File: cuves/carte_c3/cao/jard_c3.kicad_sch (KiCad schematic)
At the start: 24 parts, among them J1 Connecteur, J2 LEDs, Q1 BPC_IPP034N03L, U1 ESP32-C3_SUPERMINI_TH, U2 BPC_Alim3_3V, X1 Trou, X2 Trou

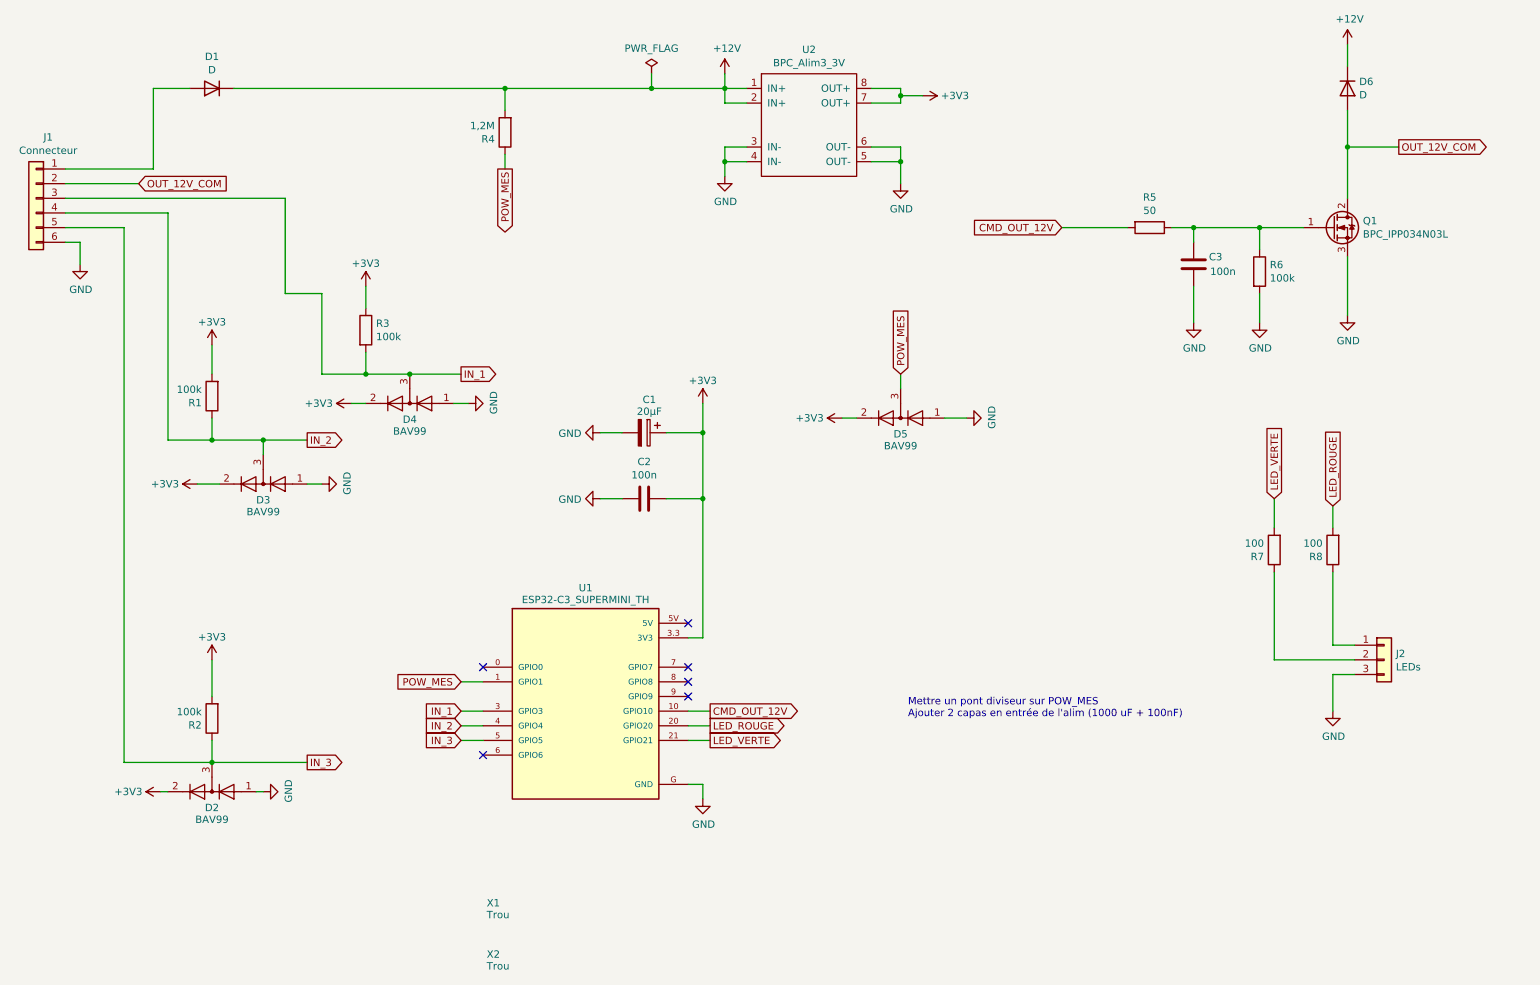
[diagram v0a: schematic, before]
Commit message: Changement de la forme de la carte: Boîte 85 x 85 x 55
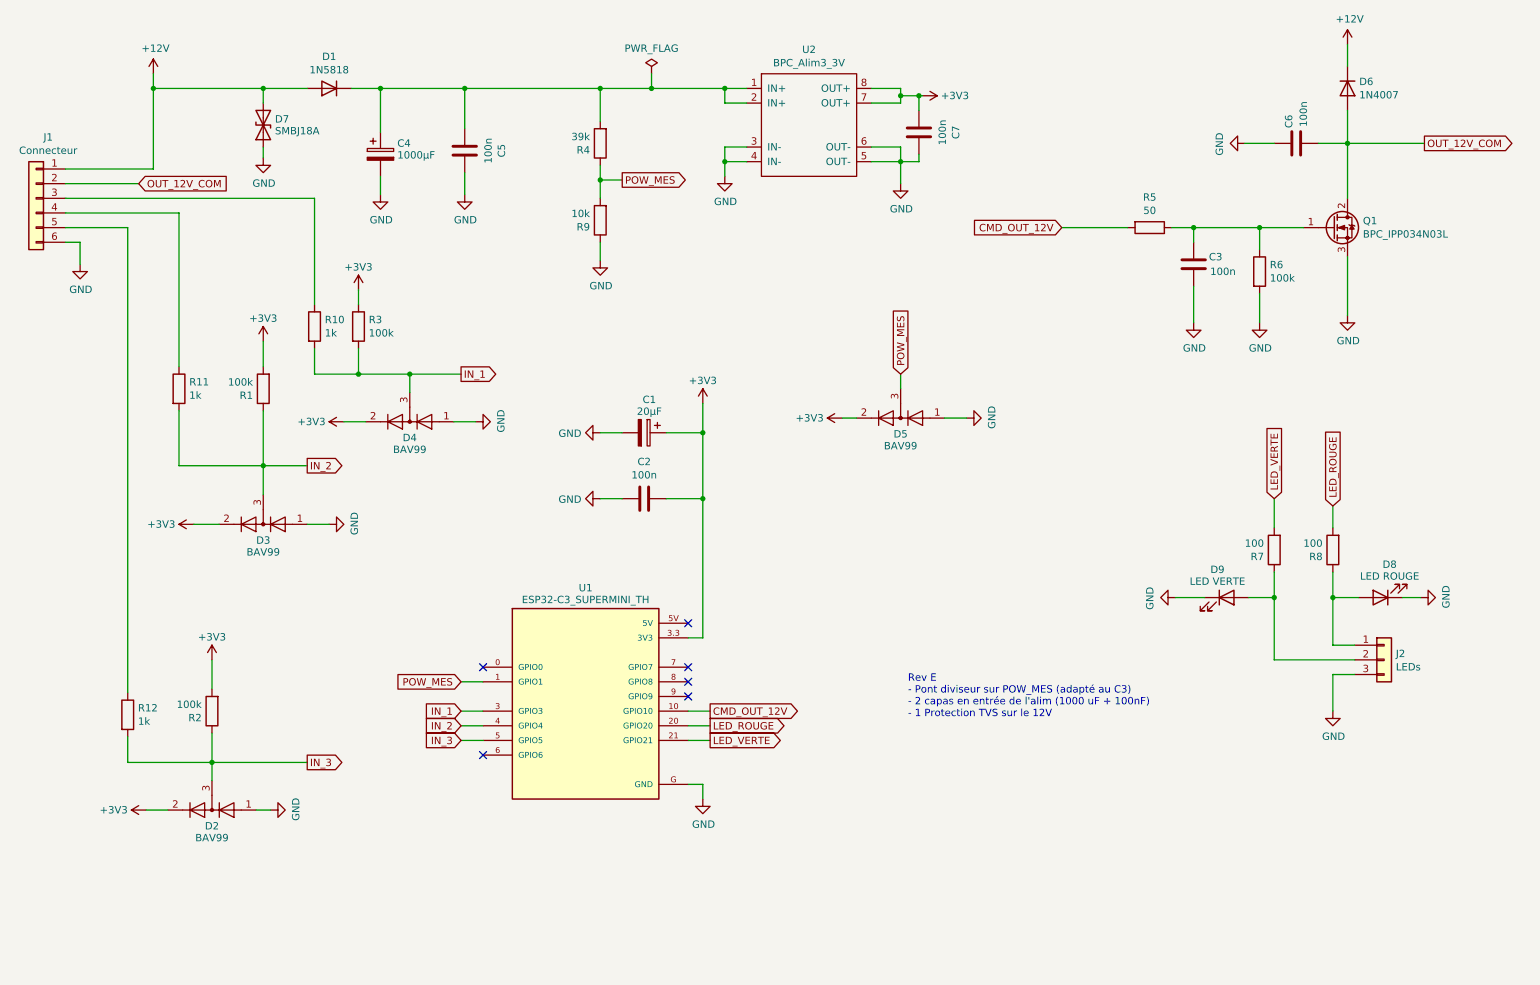
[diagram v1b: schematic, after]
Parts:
- removed X1, X2: Trou, bpc:BPC_Trou4mm_Fixation, symbol bpc:BPC_TROU
- added C4: 1000µF, Capacitor_THT:C_Radial_D16.0mm_H25.0mm_P7.50mm, symbol Device:C_Polarized
- added C5, C6, C7: 100n, Capacitor_SMD:C_0805_2012Metric_Pad1.18x1.45mm_HandSolder, symbol Device:C
- added D7: SMBJ18A, Diode_SMD:D_SMB_Handsoldering, symbol Device:D_TVS
- added D8: LED ROUGE, LED_THT:LED_D3.0mm, symbol Device:LED
- added D9: LED VERTE, LED_THT:LED_D3.0mm, symbol Device:LED
- added R10, R11, R12: 1k, Resistor_SMD:R_0805_2012Metric_Pad1.20x1.40mm_HandSolder, symbol Device:R
- added R9: 10k, Resistor_SMD:R_0805_2012Metric_Pad1.20x1.40mm_HandSolder, symbol Device:R
- D1: value D -> 1N5818; footprint Diode_THT:D_A-405_P2.54mm_Vertical_KathodeUp -> Diode_THT:D_DO-41_SOD81_P10.16mm_Horizontal
- D6: value D -> 1N4007
- R4: value 1,2M -> 39k
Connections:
- net +12V: now also D1.2 (A), J1.1 (Pin_1), D7.2 (A2); no longer D1.1 (K), R4.2, U2.1 (IN+), U2.2 (IN+)
- net +3V3: now also C7.2
- net GND: now also C4.2, C5.1, C6.1, C7.1, D7.1 (A1), D8.1 (K), D9.1 (K), R9.1
- net IN_1: now also R10.2; no longer J1.3 (Pin_3)
- net IN_2: now also R11.2; no longer J1.4 (Pin_4)
- net IN_3: now also R12.2; no longer J1.5 (Pin_5)
- net OUT_12V_COM: now also C6.2
- net POW_MES: now also R9.2
- net at J2.2 (Pin_2), R7.1: now also D9.2 (A)
- net at J2.1 (Pin_1), R8.1: now also D8.2 (A)
- new net: J1.3 (Pin_3), R10.1
- new net: J1.4 (Pin_4), R11.1
- new net: J1.5 (Pin_5), R12.1
- new net: C4.1, C5.2, D1.1 (K), R4.2, U2.1 (IN+), U2.2 (IN+)
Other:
- note added: "Rev E - Pont diviseur sur POW_MES (adapté au C3) - 2 capas en entrée de l'alim (1000 uF + 100nF) - 1 Protection TVS sur le 12V"
- note removed: "Mettre un pont diviseur sur POW_MES Ajouter 2 capas en entrée de l'alim (1000 uF + 100nF)"
- moved on the sheet: D1, D2, D3, D4, R1, R2, R3, R4

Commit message: Finalisation / règles kicad...
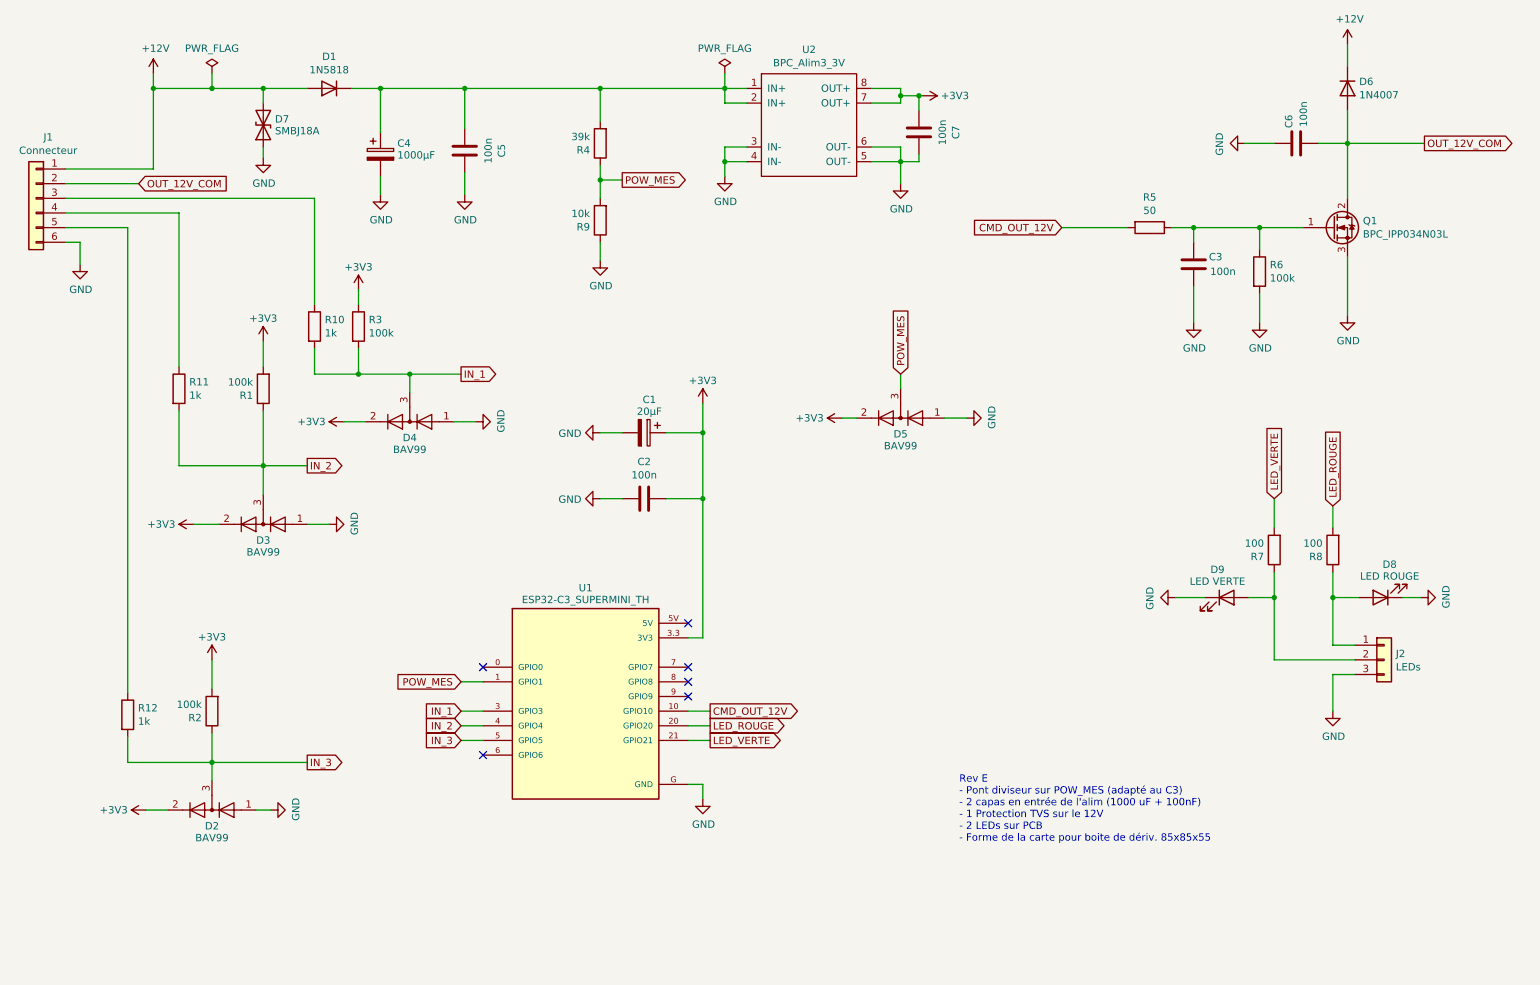
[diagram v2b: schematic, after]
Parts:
- D2, D3, D4, D5: footprint Package_TO_SOT_SMD:SOT-23 -> bpc:BPC_SOT-23-3_HandSoldering
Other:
- note added: "Rev E - Pont diviseur sur POW_MES (adapté au C3) - 2 capas en entrée de l'alim (1000 uF + 100nF) - 1 Protection TVS sur le 12V - 2 LEDs sur PCB - Forme de la carte pour boite de dériv. 85x85x55"
- note removed: "Rev E - Pont diviseur sur POW_MES (adapté au C3) - 2 capas en entrée de l'alim (1000 uF + 100nF) - 1 Protection TVS sur le 12V"
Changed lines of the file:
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@@
   (junction (at 218.44 52.07) (diameter 0) (color 0 0 0 0)
   )
-  (junction (at 124.46 27.94) (diameter 0) (color 0 0 0 0)
-  )
   (junction (at 133.35 87.63) (diameter 0) (color 0 0 0 0)
   )
@@
   )
   (junction (at 242.57 116.205) (diameter 0) (color 0 0 0 0)
+  )
+  (junction (at 48.26 27.94) (diameter 0) (color 0 0 0 0)
   )
   (junction (at 57.15 27.94) (diameter 0) (color 0 0 0 0)
@@
     (stroke (width 0) (type default))
   )
+  (wire (pts (xy 48.26 27.94) (xy 57.15 27.94))
+    (stroke (width 0) (type default))
+  )
   (wire (pts (xy 42.545 93.345) (xy 57.15 93.345))
     (stroke (width 0) (type default))
@@
     (stroke (width 0) (type default))
   )
-  (wire (pts (xy 115.57 27.94) (xy 124.46 27.94))
-    (stroke (width 0) (type default))
-  )
   (wire (pts (xy 115.57 99.06) (xy 119.38 99.06))
     (stroke (width 0) (type default))
@@
     (stroke (width 0) (type default))
   )
+  (wire (pts (xy 137.16 25.4) (xy 137.16 27.94))
+    (stroke (width 0) (type default))
+  )
   (wire (pts (xy 162.56 27.94) (xy 167.64 27.94))
     (stroke (width 0) (type default))
@@
     (stroke (width 0) (type default))
   )
-  (wire (pts (xy 124.46 25.4) (xy 124.46 27.94))
-    (stroke (width 0) (type default))
-  )
   (wire (pts (xy 133.35 148.59) (xy 133.35 151.13))
     (stroke (width 0) (type default))
@@
     (stroke (width 0) (type default))
   )
-  (wire (pts (xy 124.46 27.94) (xy 137.16 27.94))
+  (wire (pts (xy 115.57 27.94) (xy 137.16 27.94))
     (stroke (width 0) (type default))
   )
@@
     (stroke (width 0) (type default))
   )
+  (wire (pts (xy 48.26 25.4) (xy 48.26 27.94))
+    (stroke (width 0) (type default))
+  )
   (wire (pts (xy 167.64 40.64) (xy 167.64 44.45))
     (stroke (width 0) (type default))
@@
     (stroke (width 0) (type default))
   )
-  (wire (pts (xy 38.1 27.94) (xy 57.15 27.94))
+  (wire (pts (xy 38.1 27.94) (xy 48.26 27.94))
     (stroke (width 0) (type default))
   )
@@
     (stroke (width 0) (type default))
   )
-  (text "Rev E\n- Pont diviseur sur POW_MES (adapté au C3)\n- 2 capas en entrée de l'alim (1000 uF + 100nF)\n- 1 Protection TVS sur le 12V"
-    (at 168.91 137.16 0)
+  (text "Rev E\n- Pont diviseur sur POW_MES (adapté au C3)\n- 2 capas en entrée de l'alim (1000 uF + 100nF)\n- 1 Protection TVS sur le 12V\n- 2 LEDs sur PCB\n- Forme de la carte pour boite de dériv. 85x85x55"
+    (at 177.8 158.75 0)
     (effects (font (size 1.27 1.27)) (justify left bottom))
   )
@@
     )
   )
-  (symbol (lib_id "power:PWR_FLAG") (at 124.46 25.4 0) (unit 1)
-    (in_bom yes) (on_board yes) (dnp no)
-    (property "Reference" "#FLG01" (at 124.46 23.495 0)
-      (effects (font (size 1.27 1.27)) hide)
-    )
-    (property "Value" "PWR_FLAG" (at 124.46 21.0058 0)
-      (effects (font (size 1.27 1.27)))
-    )
-    (property "Footprint" "" (at 124.46 25.4 0)
-      (effects (font (size 1.27 1.27)) hide)
-    )
-    (property "Datasheet" "~" (at 124.46 25.4 0)
+  (symbol (lib_id "power:PWR_FLAG") (at 48.26 25.4 0) (unit 1)
+    (in_bom yes) (on_board yes) (dnp no)
+    (property "Reference" "#FLG01" (at 48.26 23.495 0)
+      (effects (font (size 1.27 1.27)) hide)
+    )
+    (property "Value" "PWR_FLAG" (at 48.26 21.0058 0)
+      (effects (font (size 1.27 1.27)))
+    )
+    (property "Footprint" "" (at 48.26 25.4 0)
+      (effects (font (size 1.27 1.27)) hide)
+    )
+    (property "Datasheet" "~" (at 48.26 25.4 0)
       (effects (font (size 1.27 1.27)) hide)
     )
@@
     )
   )
+  (symbol (lib_id "power:PWR_FLAG") (at 137.16 25.4 0) (unit 1)
+    (in_bom yes) (on_board yes) (dnp no)
+    (property "Reference" "#FLG02" (at 137.16 23.495 0)
+      (effects (font (size 1.27 1.27)) hide)
+    )
+    (property "Value" "PWR_FLAG" (at 137.16 21.0058 0)
+      (effects (font (size 1.27 1.27)))
+    )
+    (property "Footprint" "" (at 137.16 25.4 0)
+      (effects (font (size 1.27 1.27)) hide)
+    )
+    (property "Datasheet" "~" (at 137.16 25.4 0)
+      (effects (font (size 1.27 1.27)) hide)
+    )
+    (pin "1")
+    (instances
+      (project "jard_c3"
+        (path "/9c7bb1c5-5de0-4a64-a5e8-e95ef718eaa6"
+          (reference "#FLG02") (unit 1)
+        )
+      )
+    )
+  )
   (symbol (lib_id "Diode:BAV99") (at 167.64 85.09 180) (unit 1)
     (in_bom yes) (on_board yes) (dnp no) (fields_autoplaced)
@@
       (effects (font (size 1.27 1.27)))
     )
-    (property "Footprint" "Package_TO_SOT_SMD:SOT-23" (at 167.64 72.39 0)
+    (property "Footprint" "bpc:BPC_SOT-23-3_HandSoldering" (at 167.64 72.39 0)
       (effects (font (size 1.27 1.27)) hide)
     )
@@
       (effects (font (size 1.27 1.27)))
     )
-    (property "Footprint" "Package_TO_SOT_SMD:SOT-23" (at 82.55 73.025 0)
+    (property "Footprint" "bpc:BPC_SOT-23-3_HandSoldering" (at 82.55 73.025 0)
       (effects (font (size 1.27 1.27)) hide)
     )
@@
       (effects (font (size 1.27 1.27)))
     )
-    (property "Footprint" "Package_TO_SOT_SMD:SOT-23" (at 48.26 140.335 0)
+    (property "Footprint" "bpc:BPC_SOT-23-3_HandSoldering" (at 48.26 140.335 0)
       (effects (font (size 1.27 1.27)) hide)
     )
@@
       (effects (font (size 1.27 1.27)))
     )
-    (property "Footprint" "Package_TO_SOT_SMD:SOT-23" (at 57.15 90.805 0)
-      (effects (font (size 1.27 1.27)) hide)
-    )
+    (property "Footprint" "bpc:BPC_SOT-23-3_HandSoldering" (at 57.15 90.805 0)
+      (effects (font (size 1.27 1.27)) hide)
+    )
